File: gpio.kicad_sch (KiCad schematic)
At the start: 5 parts, among them U10 R6522, U3 MXS6551, U7 MC68B50, U8 74LS259, X2 CXO_DIP8

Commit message: Update schematic.
Pull-up resistors for 6809 signals. 74LS251 mux for 8 input pins. MIDI optoisolator. Wire up 74LS139 for RD and WR. Still many unconnected pins. TODO: connect sheets with control bus.
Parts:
- added J1, J2: DIN-5_180degree, Connector_PinHeader_2.54mm:PinHeader_1x05_P2.54mm_Vertical, symbol Connector:DIN-5_180degree
- added R1: 220, Resistor_THT:R_Axial_DIN0204_L3.6mm_D1.6mm_P5.08mm_Horizontal, symbol Device:R
- added R2: 280, Resistor_THT:R_Axial_DIN0204_L3.6mm_D1.6mm_P5.08mm_Horizontal, symbol Device:R
- added U12: HCPL-2631, Package_DIP:DIP-8_W7.62mm, symbol Isolator:HCPL-2631
- added U13: 74LS251, symbol 74xx:74LS251
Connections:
- net GND: now also J1.2, U12.5 (GND), U13.8 (GND)
- net VCC: now also U10.24 (CS1), U7.10 (CS1), U7.8 (CS0), R2.1, U12.8 (VCC), U13.16 (VCC)
- net a0: now also U13.11 (S0)
- net a1: now also U13.10 (S1)
- net a2: now also U13.9 (S2)
- net d7: now also U13.5 (Y)
- net R/~{W}: now reaches U7.13 (R/~{W})
- net R/~{W}: now also U10.22 (R/~{W}), U3.28 (R/~{W})
- net at U7.2 (Rx_Data): now also R2.2, U12.7 (VO1)
- net ~{MIDICS}: now reaches U7.9 (CS2)
- net ~{VIACS}: now reaches U10.23 (~{CS2})
- new net: J1.4, R1.2
- new net: J1.5, U12.2 (C1)
- new net: R1.1, U12.1 (A1)
- no-connect marks 0 -> 8
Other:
- moved on the sheet: U10, U7

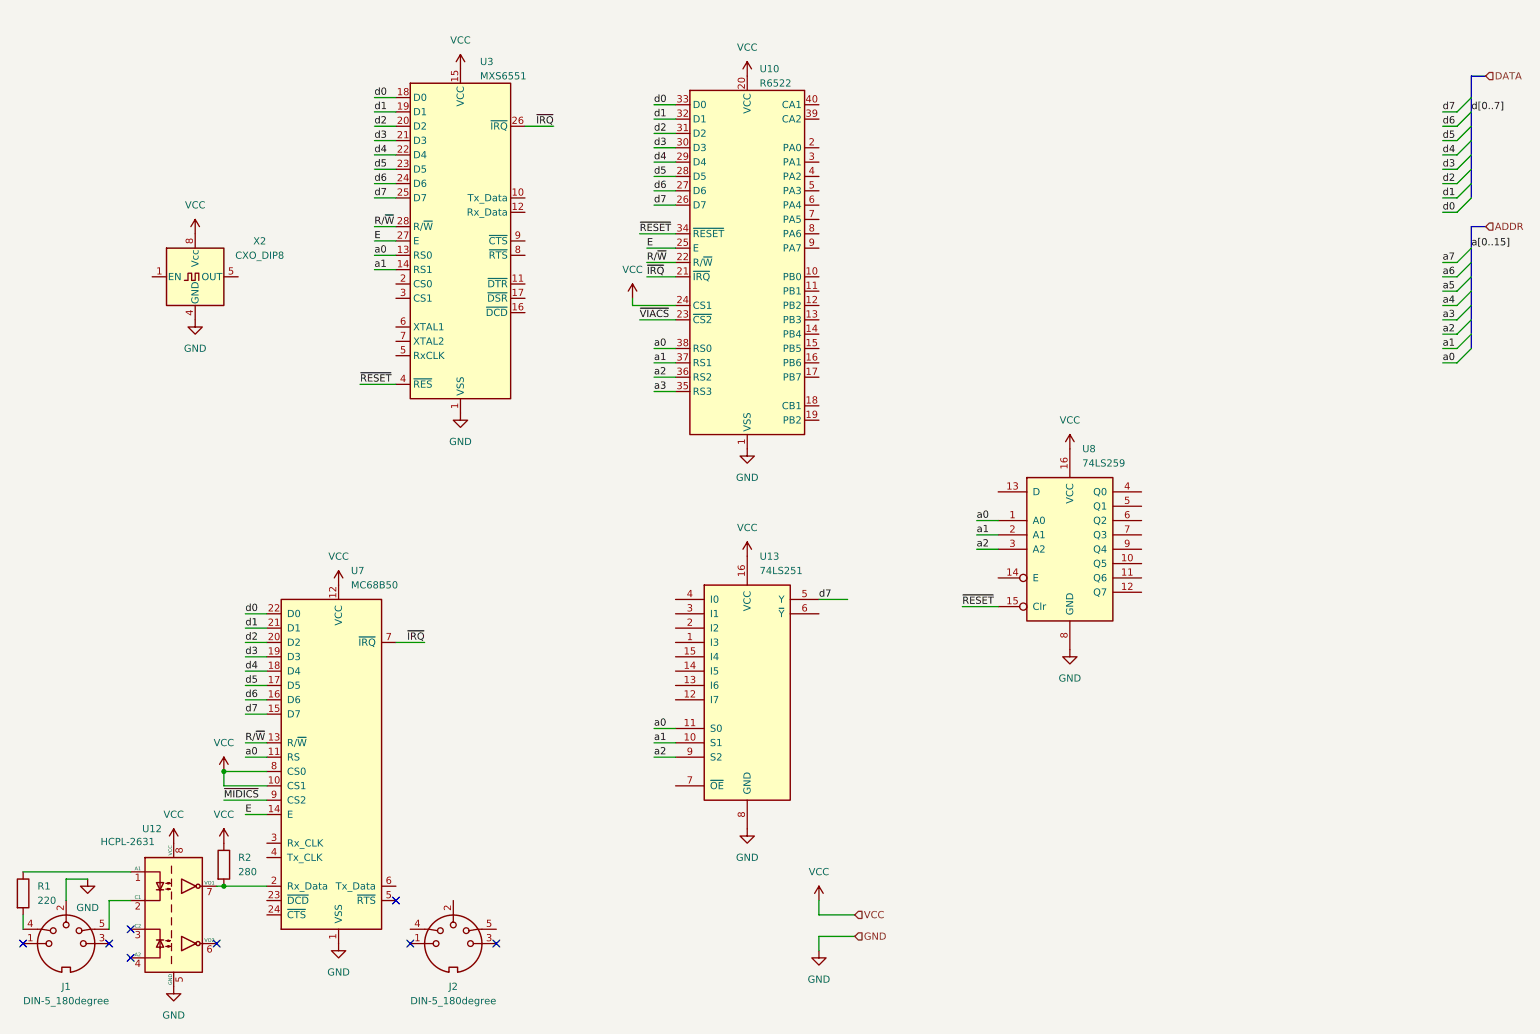
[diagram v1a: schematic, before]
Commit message: Add INTS bus, address decoder, and I2C chip.
INTS bus carries RESET, NMI, FIRQ, and IRQ. Only RESET and IRQ used so far. Philips PCF8584 I2C interface chp added. Address decoder added based on 74LS139 and two 74LS138s. TODO: add CTRL bus with E, R/W, RD, and WR.
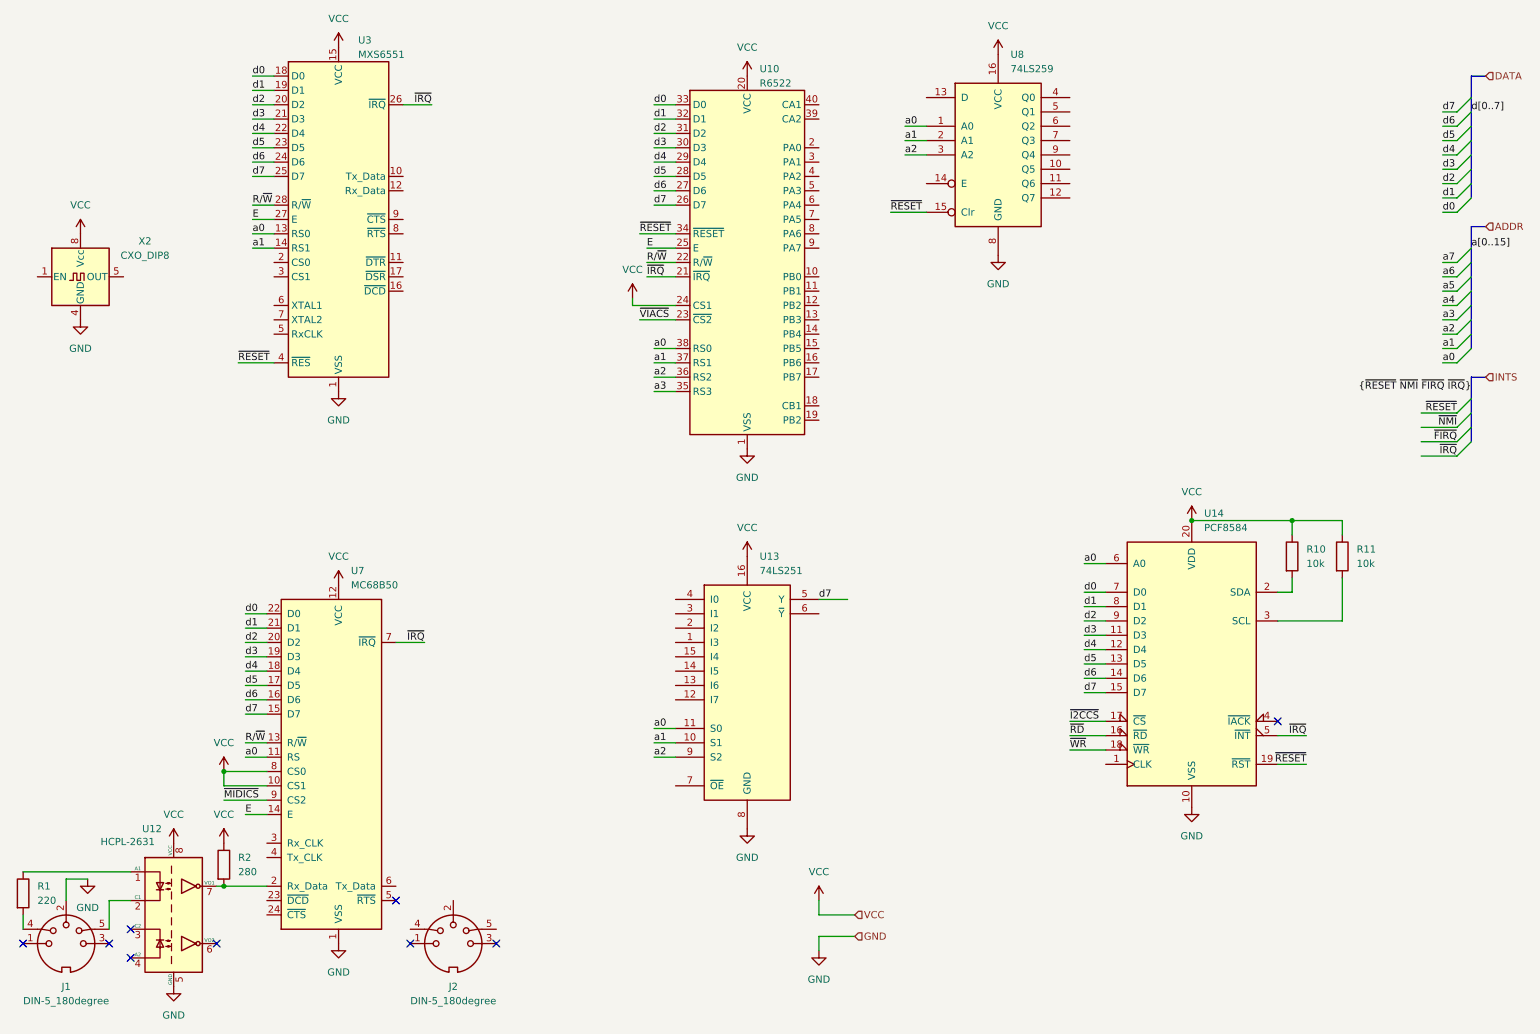
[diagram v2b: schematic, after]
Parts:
- added R10, R11: 10k, symbol Device:R
- added U14: PCF8584, symbol Interface_Expansion:PCF8584
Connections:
- net GND: now also U14.10 (VSS)
- net VCC: now also R10.1, R11.1, U14.20 (VDD)
- net a0: now also U14.6 (A0)
- net d0: now also U14.7 (D0)
- net d1: now also U14.8 (D1)
- net d2: now also U14.9 (D2)
- net d3: now also U14.11 (D3)
- net d4: now also U14.12 (D4)
- net d5: now also U14.13 (D5)
- net d6: now also U14.14 (D6)
- net d7: now also U14.15 (D7)
- net ~{IRQ}: now also U14.5 (~{INT})
- net ~{RESET}: now also U14.19 (~{RST})
- new net: R11.2, U14.3 (SCL)
- new net: R10.2, U14.2 (SDA)
- new net ~{I2CCS}: U14.17 (~{CS})
- new net ~{RD}: U14.16 (~{RD})
- new net ~{WR}: U14.18 (~{WR})
- no-connect marks 8 -> 9
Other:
- moved on the sheet: U3, U8, X2

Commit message: Add control bus.
R/W, E, RD, WR signals from microprocessor to GPIO.
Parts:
- U13: footprint (none) -> Package_DIP:DIP-16_W7.62mm
- U14: footprint (none) -> Package_DIP:DIP-20_W7.62mm
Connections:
- net ~{RD}: now also U13.7 (~{OE})
- net ~{WR}: now also U8.14 (E)

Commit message: Replace 6551 with R65C52 (dual ACIA).
New symbol for R65C52 in library. Two async serial ports in one 40-pin package. But it has no 'E' input. Also remove two misconnected WR and RD pins.
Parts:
- removed U3: MXS6551, Package_DIP:DIP-28_W15.24mm, symbol Octuplex:MXS6551
- added U3: R65C52, Package_DIP:DIP-40_W15.24mm, symbol Octuplex:R65C52
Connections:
- net GND: now also U3.20 (VSS)
- net R/~{W}: now also U3.38 (R/~{W})
- net VCC: now also U3.40 (VCC)
- net a0: now also U3.35 (RS0)
- net a1: now also U3.36 (RS1)
- net a2: now also U3.37 (RS2)
- net d0: now also U3.24 (D0)
- net d1: now also U3.23 (D1)
- net d2: now also U3.22 (D2)
- net d3: now also U3.21 (D3)
- net d4: now also U3.19 (D4)
- net d5: now also U3.18 (D5)
- net d6: now also U3.17 (D6)
- net d7: now also U3.16 (D7)
- net ~{IRQ}: now also U3.11 (~{IRQ2}), U3.29 (~{IRQ1})
- net ~{RD}: no longer U13.7 (~{OE})
- net ~{RESET}: now also U3.1 (~{RESET})
- net ~{WR}: no longer U8.14 (E)
- new net ~{DACIACS}: U3.39 (CS)

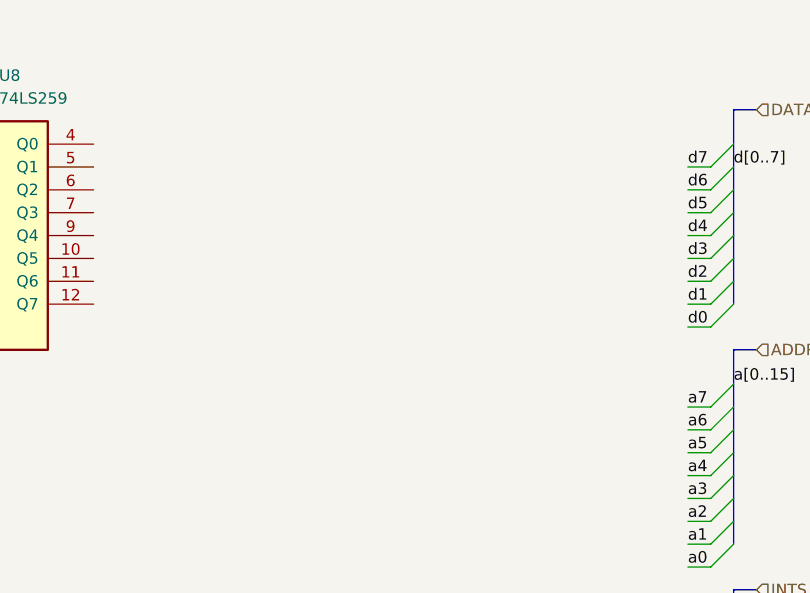
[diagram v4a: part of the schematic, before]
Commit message: Add ZN428 8-bit DAC.
Add symbol for ZN428 and place it on the GPIO page.
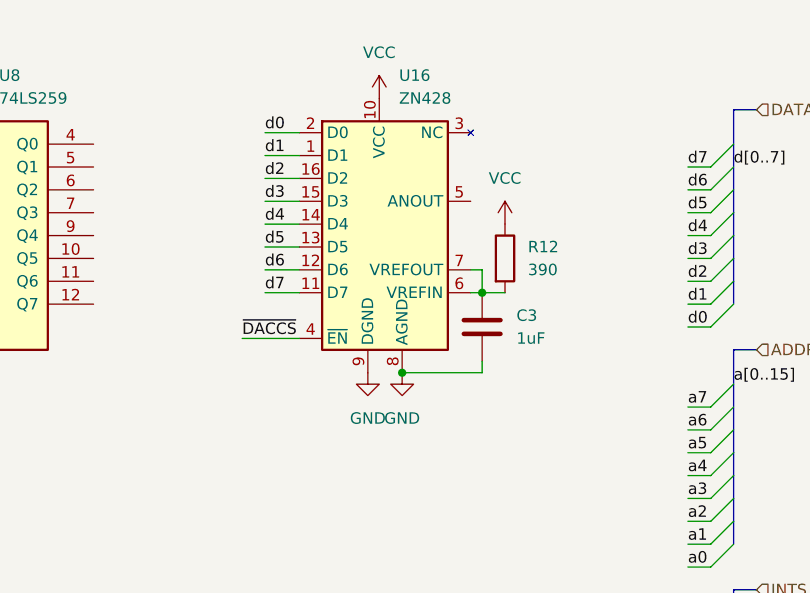
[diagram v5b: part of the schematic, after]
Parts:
- added C3: 1uF, symbol Device:C
- added R12: 390, symbol Device:R
- added U16: ZN428, Package_DIP:DIP-16_W7.62mm, symbol Octuplex:ZN428
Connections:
- net GND: now also C3.2, U16.8 (AGND), U16.9 (DGND)
- net VCC: now also R12.1, U16.10 (VCC)
- net d0: now also U16.2 (D0)
- net d1: now also U16.1 (D1)
- net d2: now also U16.16 (D2)
- net d3: now also U16.15 (D3)
- net d4: now also U16.14 (D4)
- net d5: now also U16.13 (D5)
- net d6: now also U16.12 (D6)
- net d7: now also U16.11 (D7)
- new net: C3.1, R12.2, U16.6 (VREFIN), U16.7 (VREFOUT)
- new net ~{DACCS}: U16.4 (~{EN})
